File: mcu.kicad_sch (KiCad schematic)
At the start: 8 parts, among them J20 LOLIN-S3 (L), J21 LOLIN-S3 (R), J22 ESP32-S3-DEVKITC-1 (L), J23 ESP32-S3-DEVKITC-1 (R), J24 LOLIN-S3-MINI (L), J25 LOLIN-S3-MINI (R), J26 LOLIN-S2-MINI (L), J27 LOLIN-S2-MINI (R)

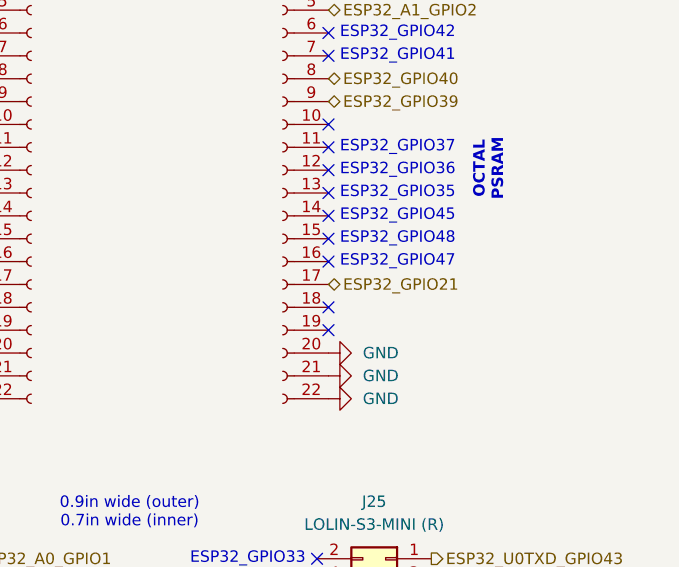
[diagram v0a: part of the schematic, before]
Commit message: Fix ESP32-S3-DEVKITC-1 bottom right pins
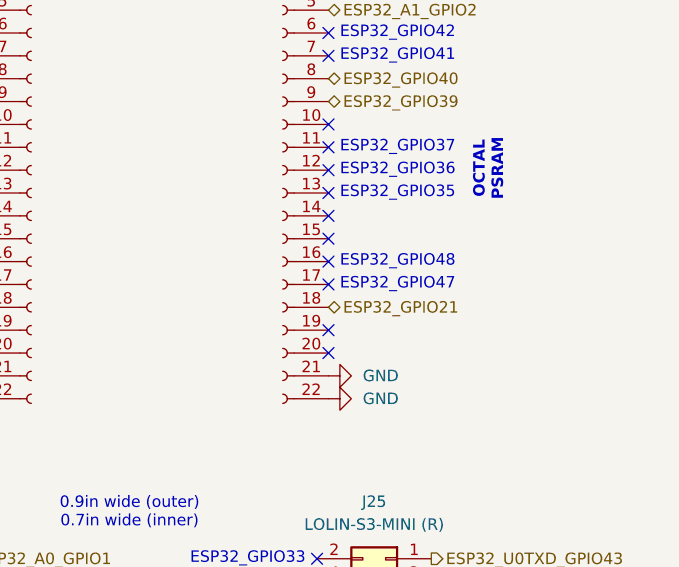
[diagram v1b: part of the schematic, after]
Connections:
- net ESP32_GPIO21: now also J23.18 (Pin_18); no longer J23.17 (Pin_17)
- net GND: no longer J23.20 (Pin_20)
- no-connect marks 39 -> 40
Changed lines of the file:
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@@
-		)
-	)
-	(text "ESP32_GPIO48"
-		(exclude_from_sim no)
-		(at 74.93 127 0)
-		(effects
-			(font
-				(size 1.27 1.27)
-			)
-			(justify left)
 		)
 	)
@@
 		)
 	)
+	(text "ESP32_GPIO42"
+		(exclude_from_sim no)
+		(at 74.93 36.83 0)
+		(effects
+			(font
+				(size 1.27 1.27)
+			)
+			(justify left)
+		)
+	)
+	(text "0.9in wide"
+		(exclude_from_sim no)
+		(at 54.61 25.908 0)
+		(effects
+			(font
+				(size 1.27 1.27)
+			)
+		)
+	)
+	(text "ESP32_GPIO42"
+		(exclude_from_sim no)
+		(at 74.93 104.14 0)
+		(effects
+			(font
+				(size 1.27 1.27)
+			)
+			(justify left)
+		)
+	)
+	(text "ESP32_GPIO36"
+		(exclude_from_sim no)
+		(at 86.36 167.64 0)
+		(effects
+			(font
+				(size 1.27 1.27)
+			)
+			(justify left)
+		)
+	)
+	(text "ESP32_GPIO34"
+		(exclude_from_sim no)
+		(at 71.12 208.28 0)
+		(effects
+			(font
+				(size 1.27 1.27)
+			)
+			(justify right)
+		)
+	)
+	(text "ESP32_GPIO47"
+		(exclude_from_sim no)
+		(at 74.93 57.15 0)
+		(effects
+			(font
+				(size 1.27 1.27)
+			)
+			(justify left)
+		)
+	)
+	(text "ESP32_GPIO37"
+		(exclude_from_sim no)
+		(at 71.12 165.1 0)
+		(effects
+			(font
+				(size 1.27 1.27)
+			)
+			(justify right)
+		)
+	)
+	(text "ESP32_GPIO35"
+		(exclude_from_sim no)
+		(at 86.36 205.74 0)
+		(effects
+			(font
+				(size 1.27 1.27)
+			)
+			(justify left)
+		)
+	)
+	(text "0.9in wide"
+		(exclude_from_sim no)
+		(at 54.102 93.218 0)
+		(effects
+			(font
+				(size 1.27 1.27)
+			)
+		)
+	)
 	(text "ESP32_GPIO45"
 		(exclude_from_sim no)
-		(at 74.93 124.46 0)
-		(effects
-			(font
-				(size 1.27 1.27)
-			)
-			(justify left)
-		)
-	)
-	(text "ESP32_GPIO42"
-		(exclude_from_sim no)
-		(at 74.93 36.83 0)
-		(effects
-			(font
-				(size 1.27 1.27)
-			)
-			(justify left)
-		)
-	)
-	(text "0.9in wide"
-		(exclude_from_sim no)
-		(at 54.61 25.908 0)
-		(effects
-			(font
-				(size 1.27 1.27)
-			)
-		)
-	)
-	(text "ESP32_GPIO42"
-		(exclude_from_sim no)
-		(at 74.93 104.14 0)
-		(effects
-			(font
-				(size 1.27 1.27)
-			)
-			(justify left)
-		)
-	)
-	(text "ESP32_GPIO36"
-		(exclude_from_sim no)
-		(at 86.36 167.64 0)
-		(effects
-			(font
-				(size 1.27 1.27)
-			)
-			(justify left)
-		)
-	)
-	(text "ESP32_GPIO34"
-		(exclude_from_sim no)
-		(at 71.12 208.28 0)
-		(effects
-			(font
-				(size 1.27 1.27)
-			)
-			(justify right)
+		(at 74.93 52.07 0)
+		(effects
+			(font
+				(size 1.27 1.27)
+			)
+			(justify left)
+		)
+	)
+	(text "ESP32_GPIO35"
+		(exclude_from_sim no)
+		(at 74.93 121.92 0)
+		(effects
+			(font
+				(size 1.27 1.27)
+			)
+			(justify left)
+		)
+	)
+	(text "ESP32_GPIO48"
+		(exclude_from_sim no)
+		(at 74.93 54.61 0)
+		(effects
+			(font
+				(size 1.27 1.27)
+			)
+			(justify left)
+		)
+	)
+	(text "ESP32_GPIO48"
+		(exclude_from_sim no)
+		(at 74.93 129.54 0)
+		(effects
+			(font
+				(size 1.27 1.27)
+			)
+			(justify left)
 		)
 	)
 	(text "ESP32_GPIO47"
 		(exclude_from_sim no)
-		(at 74.93 57.15 0)
-		(effects
-			(font
-				(size 1.27 1.27)
-			)
-			(justify left)
+		(at 74.93 132.08 0)
+		(effects
+			(font
+				(size 1.27 1.27)
+			)
+			(justify left)
+		)
+	)
+	(text "ESP32_GPIO38"
+		(exclude_from_sim no)
+		(at 71.12 203.2 0)
+		(effects
+			(font
+				(size 1.27 1.27)
+			)
+			(justify right)
 		)
 	)
 	(text "ESP32_GPIO37"
 		(exclude_from_sim no)
-		(at 71.12 165.1 0)
-		(effects
-			(font
-				(size 1.27 1.27)
-			)
-			(justify right)
-		)
-	)
-	(text "ESP32_GPIO35"
-		(exclude_from_sim no)
-		(at 86.36 205.74 0)
-		(effects
-			(font
-				(size 1.27 1.27)
-			)
-			(justify left)
-		)
-	)
-	(text "0.9in wide"
-		(exclude_from_sim no)
-		(at 54.102 93.218 0)
-		(effects
-			(font
-				(size 1.27 1.27)
-			)
-		)
-	)
-	(text "ESP32_GPIO45"
-		(exclude_from_sim no)
-		(at 74.93 52.07 0)
-		(effects
-			(font
-				(size 1.27 1.27)
-			)
-			(justify left)
-		)
-	)
-	(text "ESP32_GPIO35"
-		(exclude_from_sim no)
-		(at 74.93 121.92 0)
-		(effects
-			(font
-				(size 1.27 1.27)
-			)
-			(justify left)
-		)
-	)
-	(text "ESP32_GPIO47"
-		(exclude_from_sim no)
-		(at 74.93 129.54 0)
-		(effects
-			(font
-				(size 1.27 1.27)
-			)
-			(justify left)
-		)
-	)
-	(text "ESP32_GPIO48"
-		(exclude_from_sim no)
-		(at 74.93 54.61 0)
-		(effects
-			(font
-				(size 1.27 1.27)
-			)
-			(justify left)
-		)
-	)
-	(text "ESP32_GPIO38"
-		(exclude_from_sim no)
-		(at 71.12 203.2 0)
-		(effects
-			(font
-				(size 1.27 1.27)
-			)
-			(justify right)
-		)
-	)
-	(text "ESP32_GPIO37"
-		(exclude_from_sim no)
 		(at 86.36 203.2 0)
 		(effects
@@
 	)
 	(no_connect
+		(at 73.66 132.08)
+	)
+	(no_connect
 		(at 73.66 119.38)
 	)
@@
 	)
 	(no_connect
-		(at 73.66 134.62)
-	)
-	(no_connect
 		(at 73.66 46.99)
 	)
@@
 	(no_connect
 		(at 85.09 167.64)
+	)
+	(no_connect
+		(at 73.66 139.7)
 	)
 	(no_connect
@@
 	(hierarchical_label "ESP32_GPIO21"
 		(shape bidirectional)
-		(at 73.66 132.08 0)
+		(at 73.66 134.62 0)
 		(effects
 			(font
@@
 					(unit 1)
 				)
-			)
-		)
-	)
-	(symbol
-		(lib_id "power:GND")
-		(at 73.66 139.7 90)
-		(unit 1)
-		(exclude_from_sim no)
-		(in_bom yes)
-		(on_board yes)
-		(dnp no)
-		(fields_autoplaced yes)
-		(property "Reference" "#PWR027"
-			(at 80.01 139.7 0)
-			(effects
-				(font
-					(size 1.27 1.27)
-				)
-				(hide yes)
-			)
-		)
-		(property "Value" "GND"
-			(at 77.47 139.6999 90)
-			(effects
-				(font
-					(size 1.27 1.27)
-				)
-				(justify right)
-			)
-		)
-		(property "Footprint" ""
-			(at 73.66 139.7 0)
-			(effects
-				(font
-					(size 1.27 1.27)
-				)
-				(hide yes)
-			)
-		)
-		(property "Datasheet" ""
-			(at 73.66 139.7 0)
-			(effects
-				(font
-					(size 1.27 1.27)
-				)
-				(hide yes)
-			)
-		)
-		(property "Description" "Power symbol creates a global label with name \"GND\" , ground"
-			(at 73.66 139.7 0)
-			(effects
-				(font
-					(size 1.27 1.27)
-				)
-				(hide yes)
-			)
-		)
-		(pin "1"
-		)
-		(instances
-			(project "dali-pcb"
-				(path "/aa7f7e07-1f39-4222-a272-c9975d033b6d/a53b6c42-facd-43a9-ae46-417ca2669247"
-					(reference "#PWR027")
-					(unit 1)
-				)

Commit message: Remove the kitchen sink
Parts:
- removed J22: ESP32-S3-DEVKITC-1 (L), Connector_PinSocket_2.54mm:PinSocket_1x22_P2.54mm_Vertical, symbol Connector:Conn_01x22_Socket
- removed J23: ESP32-S3-DEVKITC-1 (R), Connector_PinSocket_2.54mm:PinSocket_1x22_P2.54mm_Vertical, symbol Connector:Conn_01x22_Socket
- removed J24: LOLIN-S3-MINI (L), Connector_PinSocket_2.54mm:PinSocket_2x08_P2.54mm_Vertical, symbol Connector_Generic:Conn_02x08_Odd_Even
- removed J25: LOLIN-S3-MINI (R), Connector_PinSocket_2.54mm:PinSocket_2x08_P2.54mm_Vertical, symbol Connector_Generic:Conn_02x08_Odd_Even
- removed J26: LOLIN-S2-MINI (L), Connector_PinSocket_2.54mm:PinSocket_2x08_P2.54mm_Vertical, symbol Connector_Generic:Conn_02x08_Odd_Even
- removed J27: LOLIN-S2-MINI (R), Connector_PinSocket_2.54mm:PinSocket_2x08_P2.54mm_Vertical, symbol Connector_Generic:Conn_02x08_Odd_Even
- renumbered J20 to J5, J21 to J6
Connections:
- net ESP32_GPIO42: now reaches J6.6 (Pin_6)
- net ESP32_GPIO41: now reaches J6.7 (Pin_7)
- net ESP32_U0RXD_GPIO44: no longer names the net of J6.5 (Pin_5)
- net ESP32_U0TXD_GPIO43: no longer names the net of J6.4 (Pin_4)
- no-connect marks 40 -> 10
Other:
- note added: "ESP32_U0RXD_GPIO44"
- note added: "ESP32_U0TXD_GPIO43"
- note removed: "0.9in wide (outer) 0.7in wide (inner)"
- note removed: "ESP32_GPIO33"
- note removed: "ESP32_GPIO34"
- note removed: "ESP32_GPIO35"
- note removed: "ESP32_GPIO36"
- note removed: "ESP32_GPIO37"
- note removed: "ESP32_GPIO38"
- note removed: "ESP32_GPIO41"
- note removed: "ESP32_GPIO42"
- note removed: "OCTAL PSRAM"
- moved on the sheet: J5, J6
